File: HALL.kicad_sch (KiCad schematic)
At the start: 0 parts

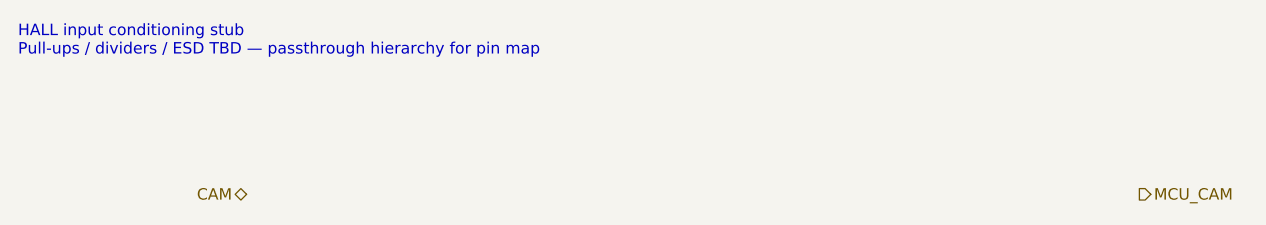
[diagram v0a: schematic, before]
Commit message: Rev e: nest INJ/LS DPAKs on frame, apply netlist, GND pours, route
Place Q1-Q7 + R1-R7 clear of AMPSEAL keepout; unify GND global net;
assign schematic nets to pads; add F/B GND zones and scripted frame
tracks/vias. Module copper remains Create Board gerber merge.
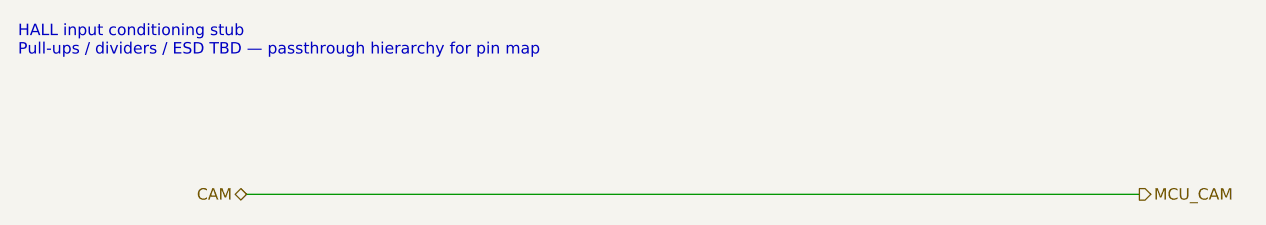
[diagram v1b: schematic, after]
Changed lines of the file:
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@@
+		)
+	)
+	(wire
+		(pts
+			(xy 50.8 30.48) (xy 150 30.48)
+		)
+		(stroke
+			(width 0)
+			(type default)
 		)
 	)
